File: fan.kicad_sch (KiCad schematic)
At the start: 8 parts, among them J10 Conn_01x04, J2 Conn_01x02, J7 Conn_01x04, J9 Conn_01x04

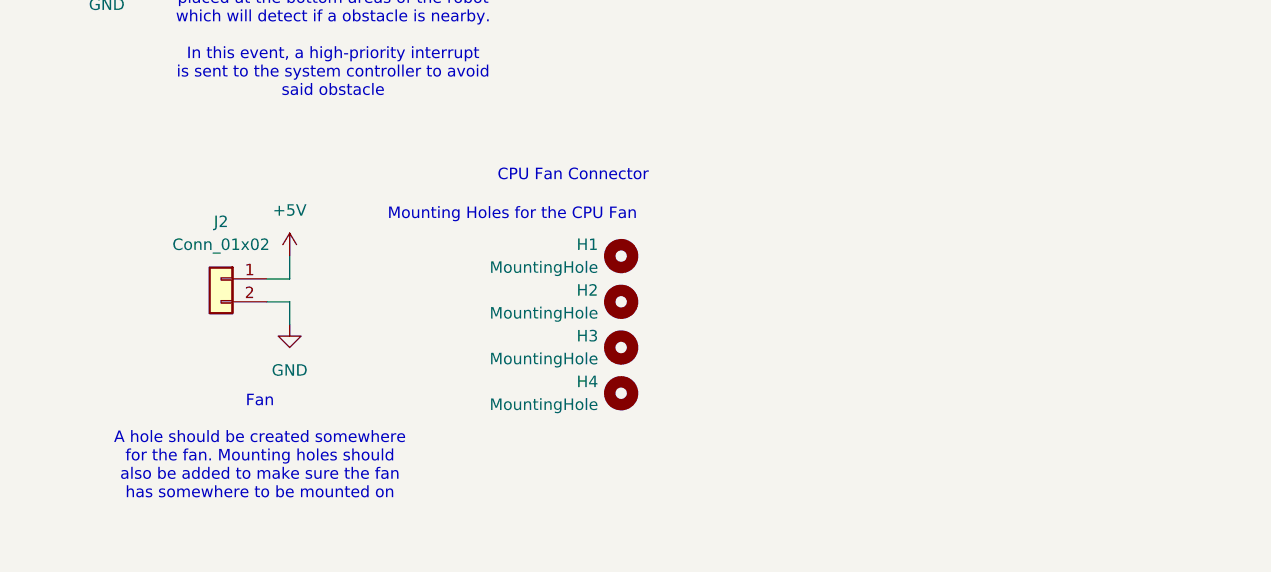
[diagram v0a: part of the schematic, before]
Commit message: feat(pcb): made the fan controlled by a NPN transistor
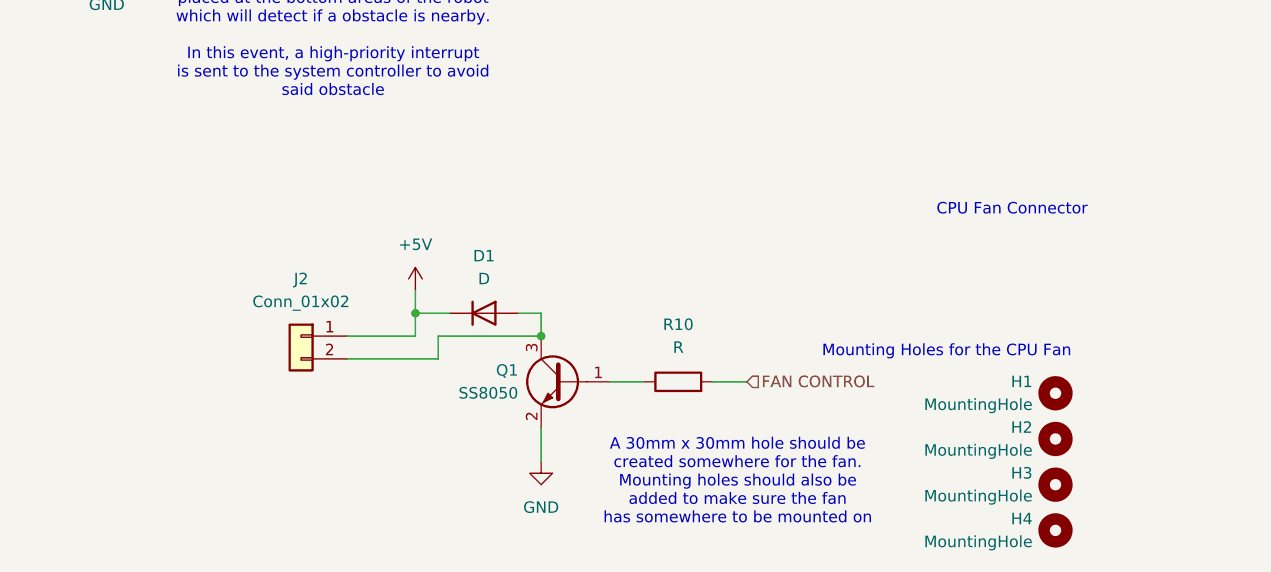
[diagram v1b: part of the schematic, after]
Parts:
- added D1: D, symbol Device:D
- added Q1: SS8050, Package_TO_SOT_SMD:SOT-23, symbol Transistor_BJT:SS8050
- added R10: R, symbol Device:R
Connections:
- net +5V: now also D1.1 (K)
- net GND: now also Q1.2 (E); no longer J2.2 (Pin_2)
- new net: Q1.1 (B), R10.1
- new net: D1.2 (A), J2.2 (Pin_2), Q1.3 (C)
- new net FAN CONTROL: R10.2
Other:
- note added: "A 30mm x 30mm hole should be created somewhere for the fan. Mounting holes should also be added to make sure the fan has somewhere to be mounted on"
- note removed: "Fan A hole should be created somewhere for the fan. Mounting holes should also be added to make sure the fan has somewhere to be mounted on"
- moved on the sheet: H1, H2, H3, H4, J2

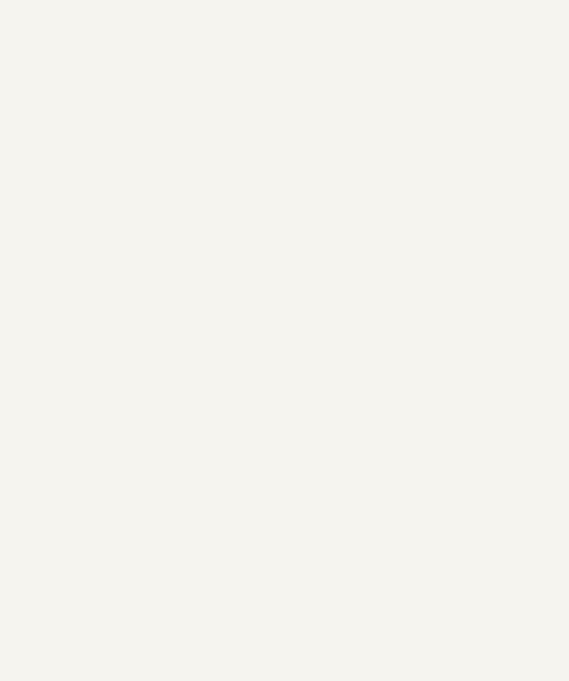
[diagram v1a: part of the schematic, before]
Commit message: chore(pcb): added IMU
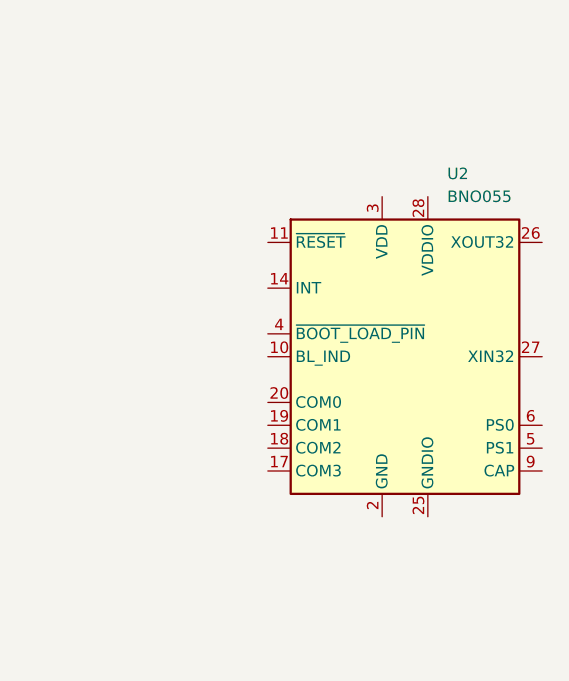
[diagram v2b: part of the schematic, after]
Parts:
- added U2: BNO055, Package_LGA:LGA-28_5.2x3.8mm_P0.5mm, symbol Sensor_Motion:BNO055
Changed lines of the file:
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@@
+		)
+	)
+	(symbol
+		(lib_id "Sensor_Motion:BNO055")
+		(at 240.03 88.9 0)
+		(unit 1)
+		(exclude_from_sim no)
+		(in_bom yes)
+		(on_board yes)
+		(dnp no)
+		(fields_autoplaced yes)
+		(property "Reference" "U2"
+			(at 244.7133 68.58 0)
+			(effects
+				(font
+					(size 1.27 1.27)
+				)
+				(justify left)
+			)
+		)
+		(property "Value" "BNO055"
+			(at 244.7133 71.12 0)
+			(effects
+				(font
+					(size 1.27 1.27)
+				)
+				(justify left)
+			)
+		)
+		(property "Footprint" "Package_LGA:LGA-28_5.2x3.8mm_P0.5mm"
+			(at 246.38 105.41 0)
+			(effects
+				(font
+					(size 1.27 1.27)
+				)
+				(justify left)
+				(hide yes)
+			)
+		)
+		(property "Datasheet" "https://www.bosch-sensortec.com/media/boschsensortec/downloads/datasheets/bst-bno055-ds000.pdf"
+			(at 240.03 83.82 0)
+			(effects
+				(font
+					(size 1.27 1.27)
+				)
+				(hide yes)
+			)
+		)
+		(property "Description" "Intelligent 9-axis absolute orientation sensor, LGA-28"
+			(at 240.03 88.9 0)
+			(effects
+				(font
+					(size 1.27 1.27)
+				)
+				(hide yes)
+			)
+		)
+		(pin "15"
+		)
+		(pin "5"
+		)
+		(pin "18"
+		)
+		(pin "22"
+		)
+		(pin "26"
+		)
+		(pin "28"
+		)
+		(pin "25"
+		)
+		(pin "6"
+		)
+		(pin "3"
+		)
+		(pin "27"
+		)
+		(pin "8"
+		)
+		(pin "1"
+		)
+		(pin "9"
+		)
+		(pin "16"
+		)
+		(pin "24"
+		)
+		(pin "23"
+		)
+		(pin "7"
+		)
+		(pin "17"
+		)
+		(pin "2"
+		)
+		(pin "21"
+		)
+		(pin "19"
+		)
+		(pin "20"
+		)
+		(pin "10"
+		)
+		(pin "4"
+		)
+		(pin "14"
+		)
+		(pin "11"
+		)
+		(pin "12"
+		)
+		(pin "13"
+		)
+		(instances
+			(project ""
+				(path "/e63e39d7-6ac0-4ffd-8aa3-1841a4541b55/c8618b48-a44a-4b17-ab33-542db64ac1dc"
+					(reference "U2")
+					(unit 1)
+				)
+			)
 		)
 	)

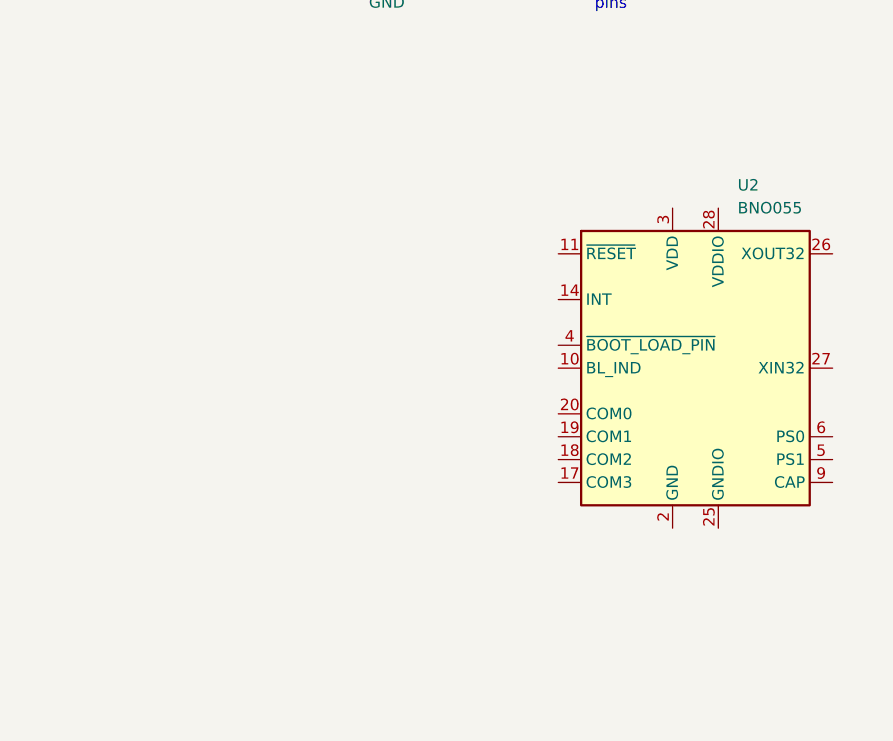
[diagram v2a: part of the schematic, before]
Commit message: feat(pcb): (somewhat) finalized all the parts needed
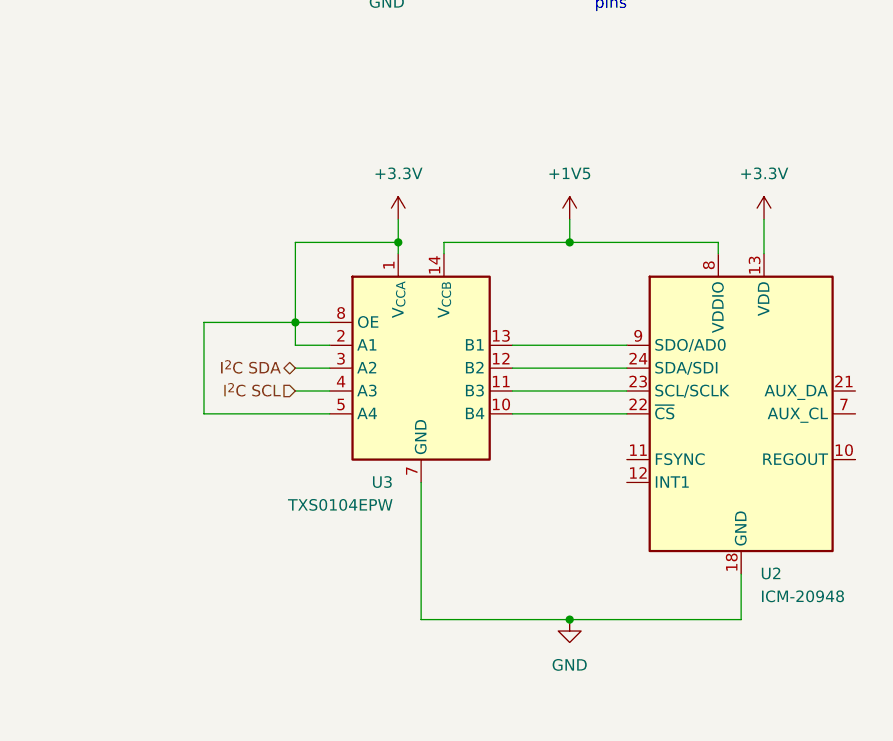
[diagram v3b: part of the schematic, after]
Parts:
- removed U2: BNO055, Package_LGA:LGA-28_5.2x3.8mm_P0.5mm, symbol Sensor_Motion:BNO055
- added U2: ICM-20948, Sensor_Motion:InvenSense_QFN-24_3x3mm_P0.4mm, symbol Sensor_Motion:ICM-20948
- added U3: TXS0104EPW, Package_SO:TSSOP-14_4.4x5mm_P0.65mm, symbol Logic_LevelTranslator:TXS0104EPW
- D1: footprint (none) -> Diode_SMD:D_SOD-323F
- J10, J7, J9: footprint (none) -> Connector_PinHeader_2.54mm:PinHeader_1x04_P2.54mm_Vertical
- R10: footprint (none) -> Resistor_SMD:R_0805_2012Metric
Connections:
- net GND: now also U2.18 (GND), U2.20 (GND), U3.7 (GND)
- new net: U2.22 (~{CS}), U3.10 (B4)
- new net: U2.23 (SCL/SCLK), U3.11 (B3)
- new net: U2.24 (SDA/SDI), U3.12 (B2)
- new net: U2.9 (SDO/AD0), U3.13 (B1)
- new net +1V5: U2.8 (VDDIO), U3.14 (V_{CCB})
- new net +3.3V: U2.13 (VDD), U3.1 (V_{CCA}), U3.2 (A1), U3.5 (A4), U3.8 (OE)
- new net I^{2}C SCL: U3.4 (A3)
- new net I^{2}C SDA: U3.3 (A2)

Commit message: feat: cleared the PCB design for a much better thingy
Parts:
- H1, H2, H3, H4: footprint Connector_JST:JST_ACH_BM01B-ACHSS-A-GAN-ETF_1x01-1MP_P1.20mm_Vertical -> MountingHole:MountingHole_2.2mm_M2
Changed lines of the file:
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@@
 			)
 		)
-		(property "Footprint" "Connector_JST:JST_ACH_BM01B-ACHSS-A-GAN-ETF_1x01-1MP_P1.20mm_Vertical"
+		(property "Footprint" "MountingHole:MountingHole_2.2mm_M2"
 			(at 147.32 110.49 0)
 			(effects
@@
 			)
 		)
-		(property "Footprint" "Connector_JST:JST_ACH_BM01B-ACHSS-A-GAN-ETF_1x01-1MP_P1.20mm_Vertical"
+		(property "Footprint" "MountingHole:MountingHole_2.2mm_M2"
 			(at 147.32 115.57 0)
 			(effects
@@
 			)
 		)
-		(property "Footprint" "Connector_JST:JST_ACH_BM01B-ACHSS-A-GAN-ETF_1x01-1MP_P1.20mm_Vertical"
+		(property "Footprint" "MountingHole:MountingHole_2.2mm_M2"
 			(at 147.32 120.65 0)
 			(effects
@@
 			)
 		)
-		(property "Footprint" "Connector_JST:JST_ACH_BM01B-ACHSS-A-GAN-ETF_1x01-1MP_P1.20mm_Vertical"
+		(property "Footprint" "MountingHole:MountingHole_2.2mm_M2"
 			(at 147.32 125.73 0)
 			(effects

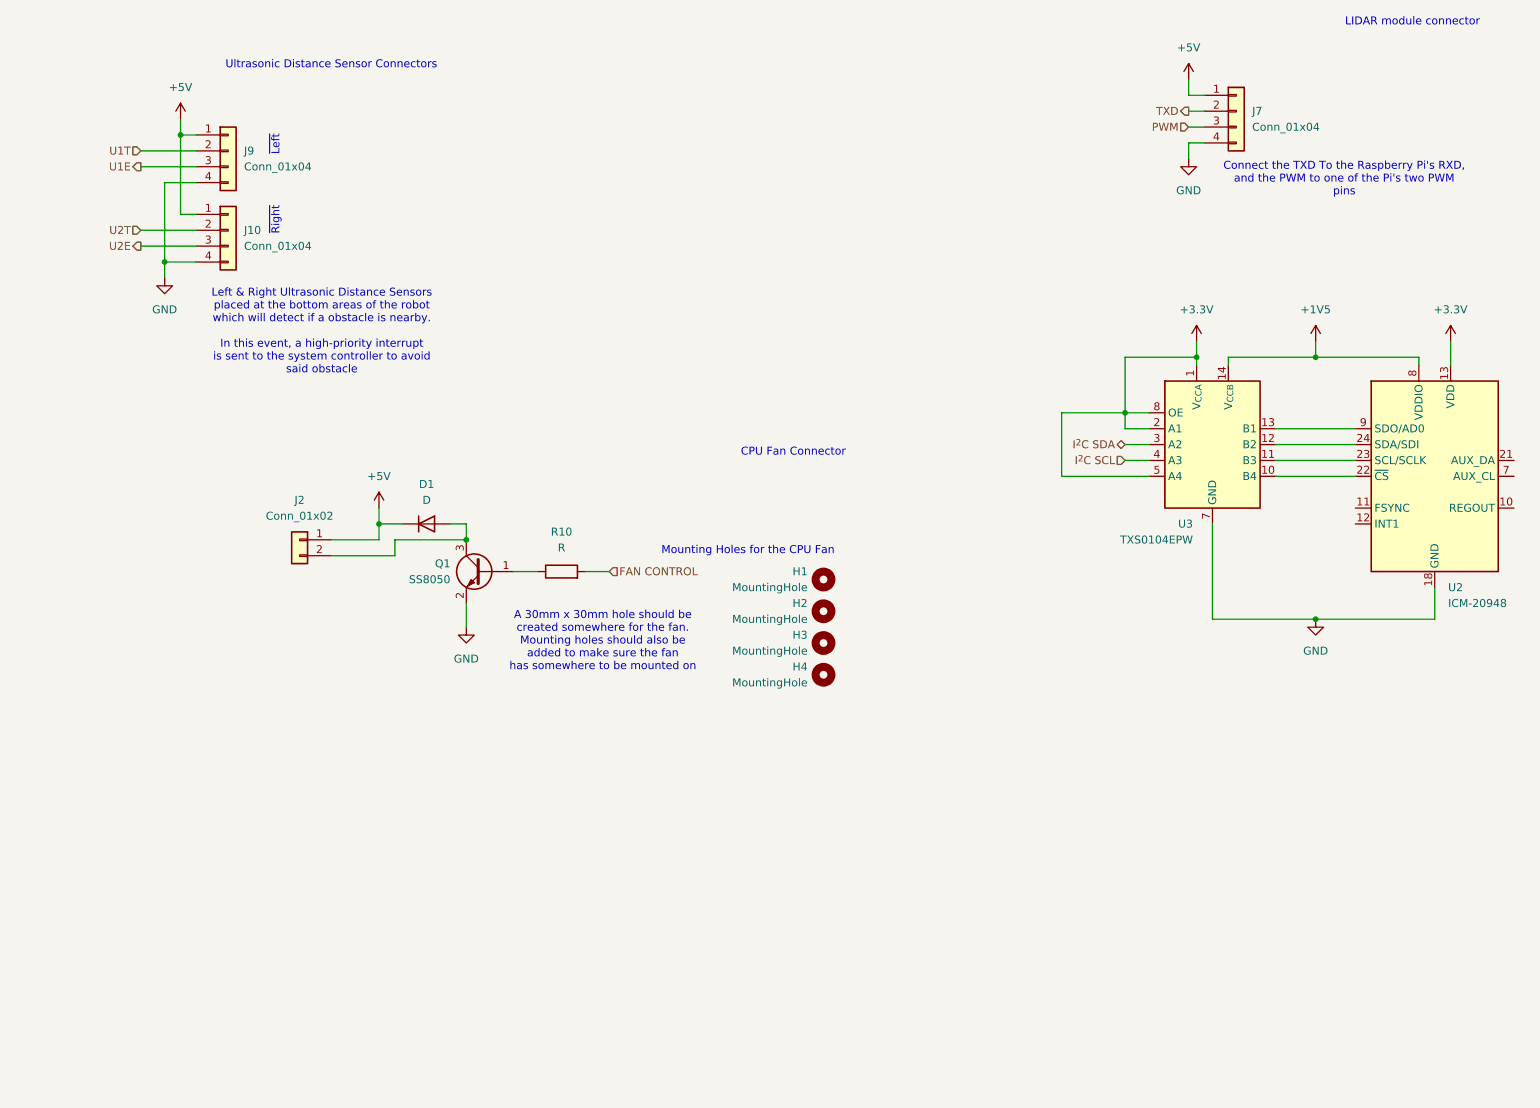
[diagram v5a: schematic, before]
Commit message: feat: added audio
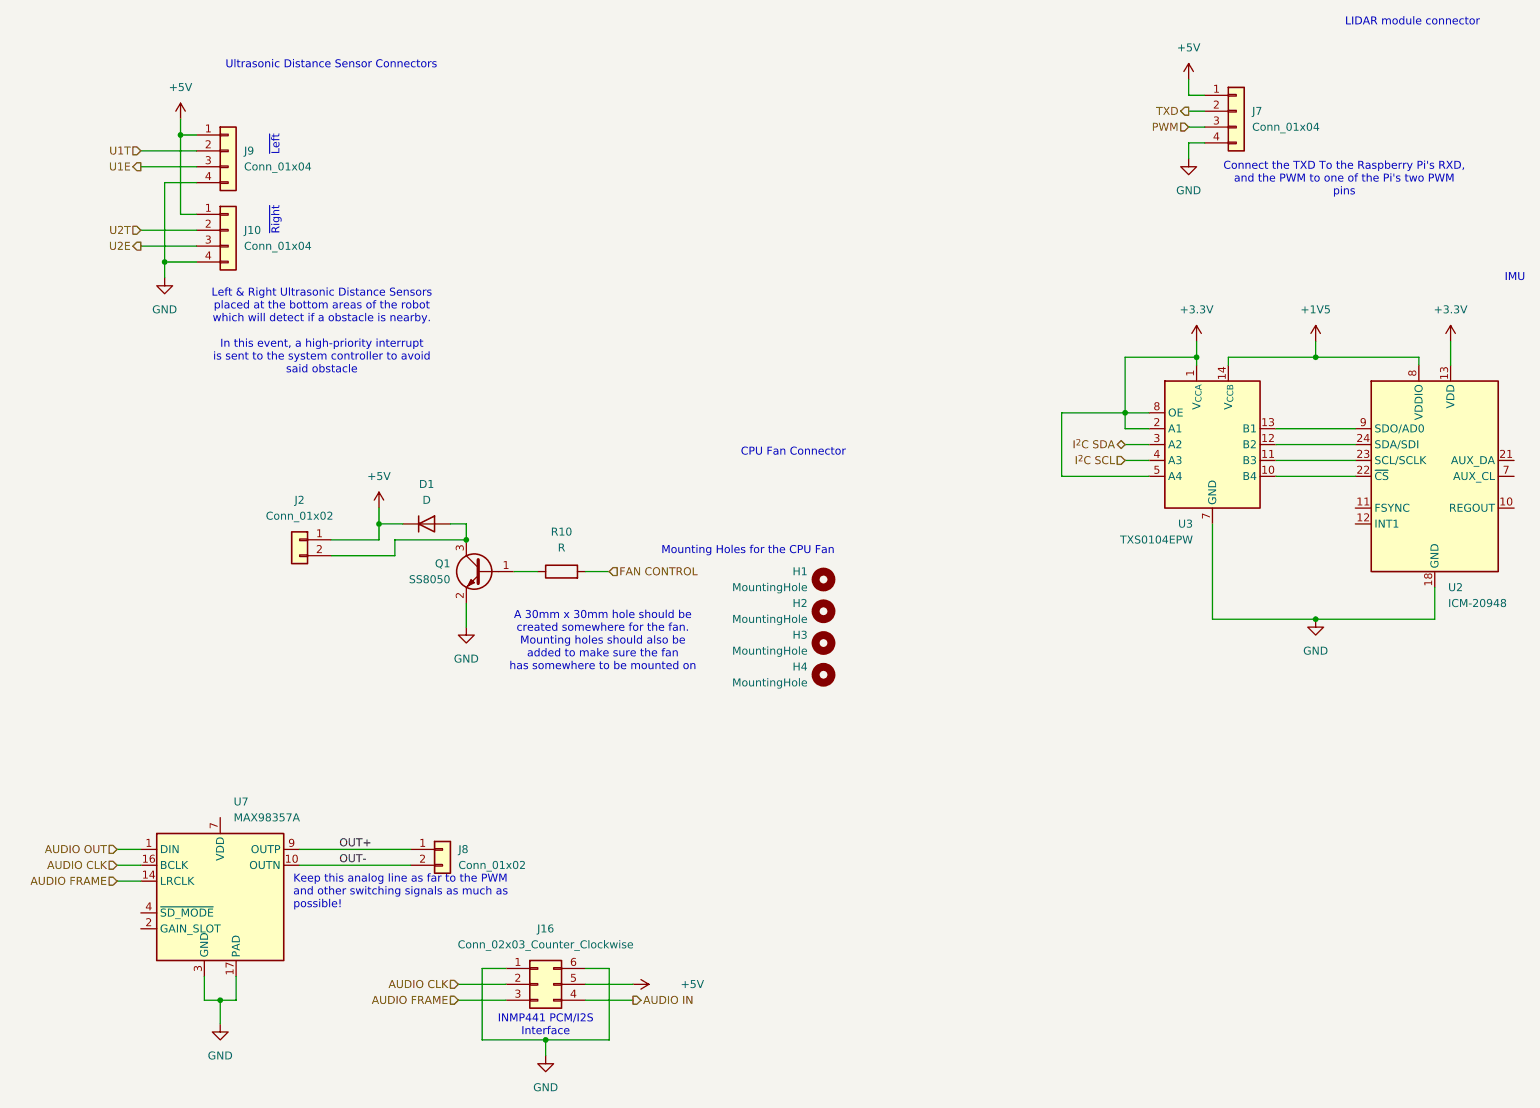
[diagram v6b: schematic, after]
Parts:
- added J16: Conn_02x03_Counter_Clockwise, symbol Connector_Generic:Conn_02x03_Counter_Clockwise
- added J8: Conn_01x02, symbol Connector_Generic:Conn_01x02
- added U7: MAX98357A, Package_DFN_QFN:TQFN-16-1EP_3x3mm_P0.5mm_EP1.23x1.23mm, symbol Audio:MAX98357A
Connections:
- net +5V: now also J16.5 (Pin_5)
- net GND: now also J16.1 (Pin_1), J16.6 (Pin_6), U7.11 (GND), U7.15 (GND), U7.17 (PAD), U7.3 (GND)
- new net: U7.7 (VDD), U7.8 (VDD)
- new net AUDIO CLK: J16.2 (Pin_2), U7.16 (BCLK)
- new net AUDIO FRAME: J16.3 (Pin_3), U7.14 (LRCLK)
- new net AUDIO IN: J16.4 (Pin_4)
- new net AUDIO OUT: U7.1 (DIN)
- new net OUT+: J8.1 (Pin_1), U7.9 (OUTP)
- new net OUT-: J8.2 (Pin_2), U7.10 (OUTN)
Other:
- note added: "IMU"
- note added: "INMP441 PCM/I2S Interface"
- note added: "Keep this analog line as far to the PWM and other switching signals as much as possible!"

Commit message: feat: basic PCB design??? i guess?
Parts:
- J2: footprint Connector_Wire:SolderWire-0.1sqmm_1x02_P3.6mm_D0.4mm_OD1mm -> Connector_PinSocket_2.54mm:PinSocket_1x02_P2.54mm_Vertical
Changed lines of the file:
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@@
 			)
 		)
-		(property "Footprint" "Connector_Wire:SolderWire-0.1sqmm_1x02_P3.6mm_D0.4mm_OD1mm"
+		(property "Footprint" "Connector_PinSocket_2.54mm:PinSocket_1x02_P2.54mm_Vertical"
 			(at 63.5 104.14 0)
 			(effects

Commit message: feat: finalized audio system
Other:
- note added: "Audio System"
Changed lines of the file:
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@@
+		)
+	)
+	(text "Audio System"
+		(exclude_from_sim no)
+		(at 122.682 142.24 0)
+		(effects
+			(font
+				(size 1.27 1.27)
+			)
 		)
 	)
@@
 			)
 			(stroke
+				(width 0)
+				(type dash)
+				(color 0 132 0 1)
+			)
+			(fill
+				(type none)
+			)
+		)
+	)
+	(rule_area
+		(polyline
+			(pts
+				(xy 18.415 143.51) (xy 18.415 194.31) (xy 128.905 194.31) (xy 128.905 143.51)
+			)
+			(stroke
